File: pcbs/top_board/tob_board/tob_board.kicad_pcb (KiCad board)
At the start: 2 copper layers, 36 x 36 mm, 10 parts, among them J1 LEDFrontLeft, J2 LEDFrontRight, J3 LEDRearLeft, J4 LEDRearRight, J5 Motor, M1 Motor_DC

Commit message: add gerbers
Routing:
- added copper zone on F.Cu, net (none)
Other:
- board text added: "top_board v0.0"
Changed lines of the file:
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@@
 		(layer "User.4")
+	)
+	(gr_text "top_board\nv0.0"
+		(at 195.87 63.93 315)
+		(layer "B.SilkS")
+		(effects
+			(font
+				(size 1 1)
+				(thickness 0.15)
+			)
+			(justify left mirror)
+		)
 	)
 	(segment
@@
 		(net 0)
 		(net_name "")
-		(layer "B.Cu")
+		(layers "F.Cu" "B.Cu")
 		(hatch edge 0.5)
 		(connect_pads

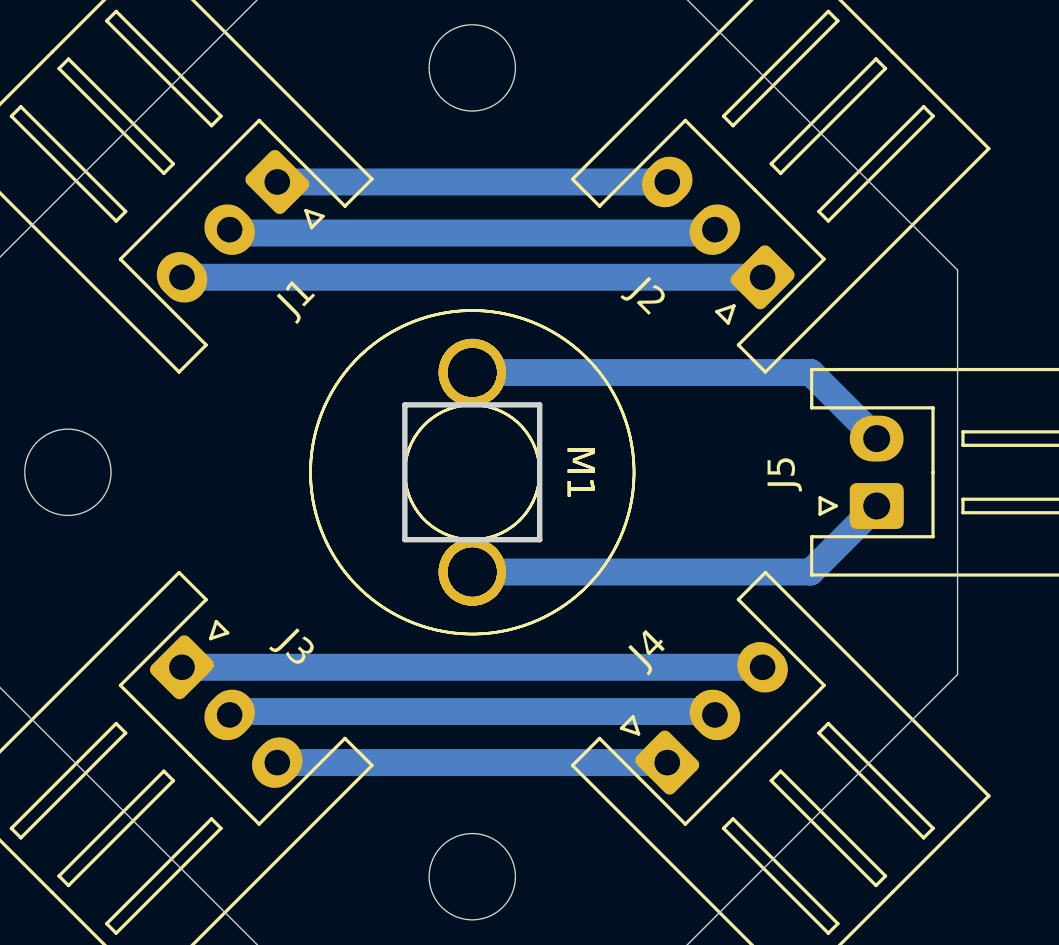
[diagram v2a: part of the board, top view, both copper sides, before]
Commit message: thicker connections for easier manufacture
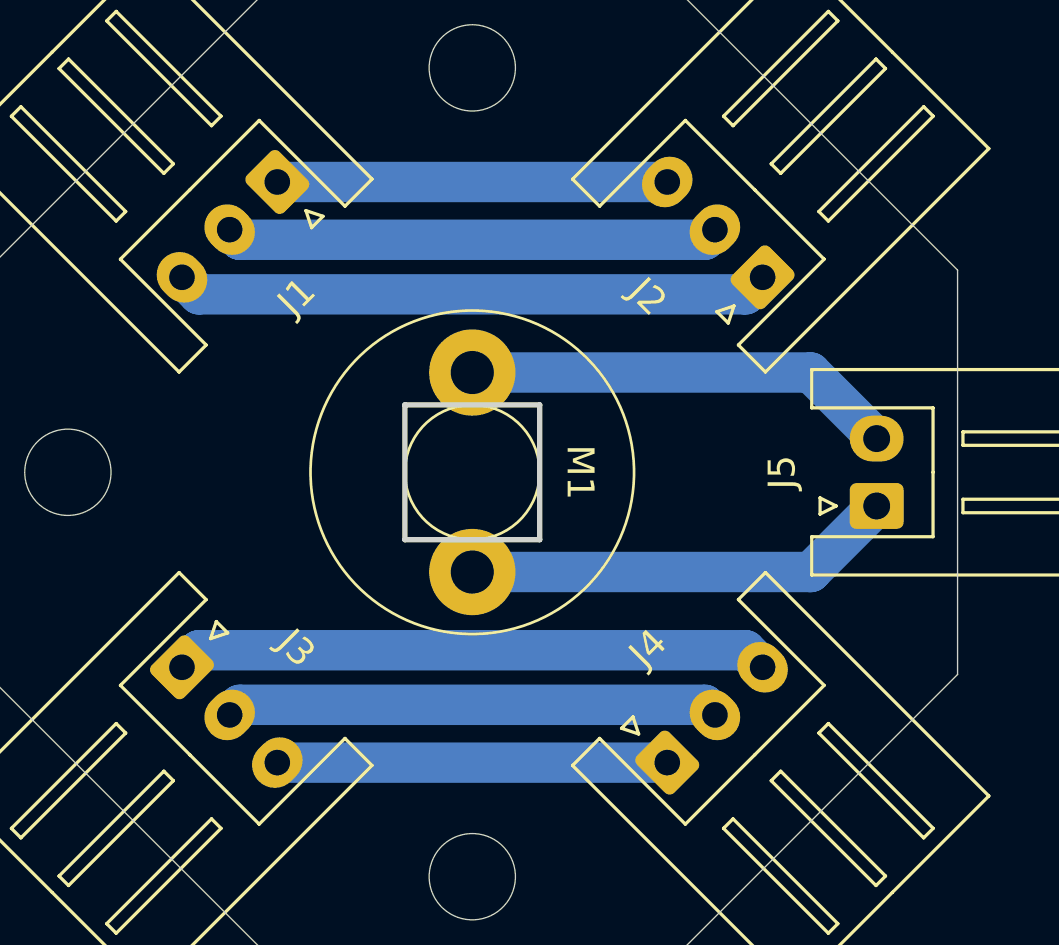
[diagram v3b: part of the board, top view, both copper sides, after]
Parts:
- removed the M1 at (180.0, 70.0)
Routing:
- net Net-(J3-Pin_1): track 21.5 -> 22.1 mm
- net Net-(J1-Pin_3): track 21.5 -> 22.1 mm
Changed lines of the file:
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@@
 		(pad "1" thru_hole circle
 			(at 0 -3.7 180)
-			(size 2.5 2.5)
-			(drill 1.8)
+			(size 3.2 3.2)
+			(drill 1.6)
 			(layers "*.Cu" "*.Mask")
 			(remove_unused_layers no)
@@
 		(pad "2" thru_hole circle
 			(at 0 3.7 180)
-			(size 2.5 2.5)
-			(drill 1.8)
+			(size 3.2 3.2)
+			(drill 1.6)
 			(layers "*.Cu" "*.Mask")
 			(remove_unused_layers no)
@@
 		)
 	)
-	(footprint "topMotor:topMotor"
-		(layer "F.Cu")
-		(at 180 70 180)
-		(property "Reference" "M1"
-			(at -4 0 270)
-			(unlocked yes)
-			(layer "F.SilkS")
-			(effects
-				(font
-					(size 1 1)
-					(thickness 0.1)
-				)
-			)
-		)
-		(property "Value" "Motor_DC"
-			(at 0 1 180)
-			(unlocked yes)
-			(layer "F.Fab")
-			(effects
-				(font
-					(size 1 1)
-					(thickness 0.15)
-				)
-			)
-		)
-		(property "Datasheet" "~"
-			(at 0 0 180)
-			(unlocked yes)
-			(layer "F.Fab")
-			(hide yes)
-			(effects
-				(font
-					(size 1 1)
-					(thickness 0.15)
-				)
-			)
-		)
-		(property "Description" "DC Motor"
-			(at 0 0 180)
-			(unlocked yes)
-			(layer "F.Fab")
-			(hide yes)
-			(effects
-				(font
-					(size 1 1)
-					(thickness 0.15)
-				)
-			)
-		)
-		(property "Manufacturer Part Number" "LA143024A"
-			(at 0 0 180)
-			(unlocked yes)
-			(layer "F.Fab")
-			(hide yes)
-			(effects
-				(font
-					(size 1 1)
-					(thickness 0.15)
-				)
-			)
-		)
-		(property "Supplier" "LaskaKit"
-			(at 0 0 180)
-			(unlocked yes)
-			(layer "F.Fab")
-			(hide yes)
-			(effects
-				(font
-					(size 1 1)
-					(thickness 0.15)
-				)
-			)
-		)
-		(property "Supplier Part Number" "LA143024A"
-			(at 0 0 180)
-			(unlocked yes)
-			(layer "F.Fab")
-			(hide yes)
-			(effects
-				(font
-					(size 1 1)
-					(thickness 0.15)
-				)
-			)
-		)
-		(property ki_fp_filters "PinHeader*P2.54mm* TerminalBlock*")
-		(sheetname "/")
-		(sheetfile "tob_board.kicad_sch")
-		(attr smd)
-		(fp_circle
-			(center 0 0)
-			(end 6 0)
-			(stroke
-				(width 0.1)
-				(type default)
-			)
-			(fill no)
-			(layer "F.SilkS")
-		)
-		(fp_circle
-			(center 0 0)
-			(end 2.5 0)
-			(stroke
-				(width 0.1)
-				(type default)
-			)
-			(fill no)
-			(layer "F.SilkS")
-		)
-		(fp_text user "${REFERENCE}"
-			(at 0 2.5 180)
-			(unlocked yes)
-			(layer "F.Fab")
-			(effects
-				(font
-					(size 1 1)
-					(thickness 0.15)
-				)
-			)
-		)
-		(pad "1" thru_hole circle
-			(at 0 -3.7 180)
-			(size 2.5 2.5)
-			(drill 1.8)
-			(layers "*.Cu" "*.Mask")
-			(remove_unused_layers no)
-			(net 8 "Net-(J5-Pin_1)")
-			(pinfunction "+")
-			(pintype "passive")
-		)
-		(pad "2" thru_hole circle
-			(at 0 3.7 180)
-			(size 2.5 2.5)
-			(drill 1.8)
-			(layers "*.Cu" "*.Mask")
-			(remove_unused_layers no)
-			(net 7 "Net-(J5-Pin_2)")
-			(pinfunction "-")
-			(pintype "passive")
-		)
-		(embedded_fonts no)
-	)
 	(footprint "MountingHole:MountingHole_3.2mm_M3"
 		(layer "F.Cu")
@@
 	)
 	(segment
-		(start 171.125047 61.125047)
-		(end 188.874953 61.125047)
-		(width 1)
+		(start 188.624953 61.375047)
+		(end 189 61)
+		(width 1.5)
 		(layer "B.Cu")
 		(net 1)
 	)
 	(segment
-		(start 171 61)
-		(end 171.125047 61.125047)
-		(width 1)
+		(start 171.375047 61.375047)
+		(end 188.624953 61.375047)
+		(width 1.5)
 		(layer "B.Cu")
 		(net 1)
 	)
 	(segment
-		(start 188.874953 61.125047)
-		(end 189 61)
-		(width 1)
+		(start 171 61)
+		(end 171.375047 61.375047)
+		(width 1.5)
 		(layer "B.Cu")
 		(net 1)
@@
 	(segment
 		(start 190.767767 62.767767)
+		(end 190.135534 63.4)
+		(width 1.5)
+		(layer "B.Cu")
+		(net 2)
+	)
+	(segment
+		(start 169.864466 63.4)
 		(end 169.232233 62.767767)
-		(width 1)
+		(width 1.5)
+		(layer "B.Cu")
+		(net 2)
+	)
+	(segment
+		(start 190.135534 63.4)
+		(end 169.864466 63.4)
+		(width 1.5)
 		(layer "B.Cu")
 		(net 2)
@@
 		(start 187.232233 59.232233)
 		(end 172.767767 59.232233)
-		(width 1)
+		(width 1.5)
 		(layer "B.Cu")
 		(net 3)
 	)
 	(segment
-		(start 190.767767 77.232233)
-		(end 169.232233 77.232233)
-		(width 1)
+		(start 190.135534 76.6)
+		(end 169.864466 76.6)
+		(width 1.5)
 		(layer "B.Cu")
 		(net 4)
 	)
 	(segment
-		(start 187.232233 80.767767)
-		(end 172.767767 80.767767)
-		(width 1)
+		(start 190.767767 77.232233)
+		(end 190.135534 76.6)
+		(width 1.5)
 		(layer "B.Cu")
-		(net 5)
+		(net 4)
 	)
 	(segment
-		(start 189 79)
-		(end 188.874953 78.874953)
-		(width 1)
-		(layer "F.Cu")
-		(net 6)
+		(start 169.864466 76.6)
+		(end 169.232233 77.232233)
+		(width 1.5)
+		(layer "B.Cu")
+		(net 4)
 	)
 	(segment
-		(start 171.125047 78.874953)
-		(end 171 79)
-		(width 1)
-		(layer "F.Cu")
-		(net 6)
+		(start 172.767767 80.767767)
+		(end 187.232233 80.767767)
+		(width 1.5)
+		(layer "B.Cu")
+		(net 5)
 	)
 	(segment
-		(start 171.125047 78.874953)
-		(end 188.874953 78.874953)
-		(width 1)
+		(start 188.624953 78.624953)
+		(end 189 79)
+		(width 1.5)
 		(layer "B.Cu")
 		(net 6)
@@
 	(segment
 		(start 171 79)
-		(end 171.125047 78.874953)
-		(width 1)
+		(end 171.375047 78.624953)
+		(width 1.5)
 		(layer "B.Cu")
 		(net 6)
 	)
 	(segment
-		(start 188.874953 78.874953)
-		(end 189 79)
-		(width 1)
+		(start 171.375047 78.624953)
+		(end 188.624953 78.624953)
+		(width 1.5)
 		(layer "B.Cu")
 		(net 6)
@@
 		(start 192.55 66.3)
 		(end 180 66.3)
-		(width 1)
+		(width 1.5)
 		(layer "B.Cu")
 		(net 7)
@@
 		(start 195 68.75)
 		(end 192.55 66.3)
-		(width 1)
+		(width 1.5)
 		(layer "B.Cu")
 		(net 7)
@@
 		(start 195 71.25)
 		(end 192.55 73.7)
-		(width 1)
+		(width 1.5)
 		(layer "B.Cu")
 		(net 8)
@@
 		(start 192.55 73.7)
 		(end 180 73.7)
-		(width 1)
+		(width 1.5)
 		(layer "B.Cu")
 		(net 8)
